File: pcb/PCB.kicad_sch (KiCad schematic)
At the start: 35 parts, among them J1 Conn_01x15, J2 USB_C_Receptacle_USB2.0, J3 Conn_01x15, J4 TC2030, J5 Conn_01x04, SW1 SW_Push, SW2 SW_Push, U1 SN65HVD230, U2 AMS1117-3.3, U3 STM32F103C8T6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

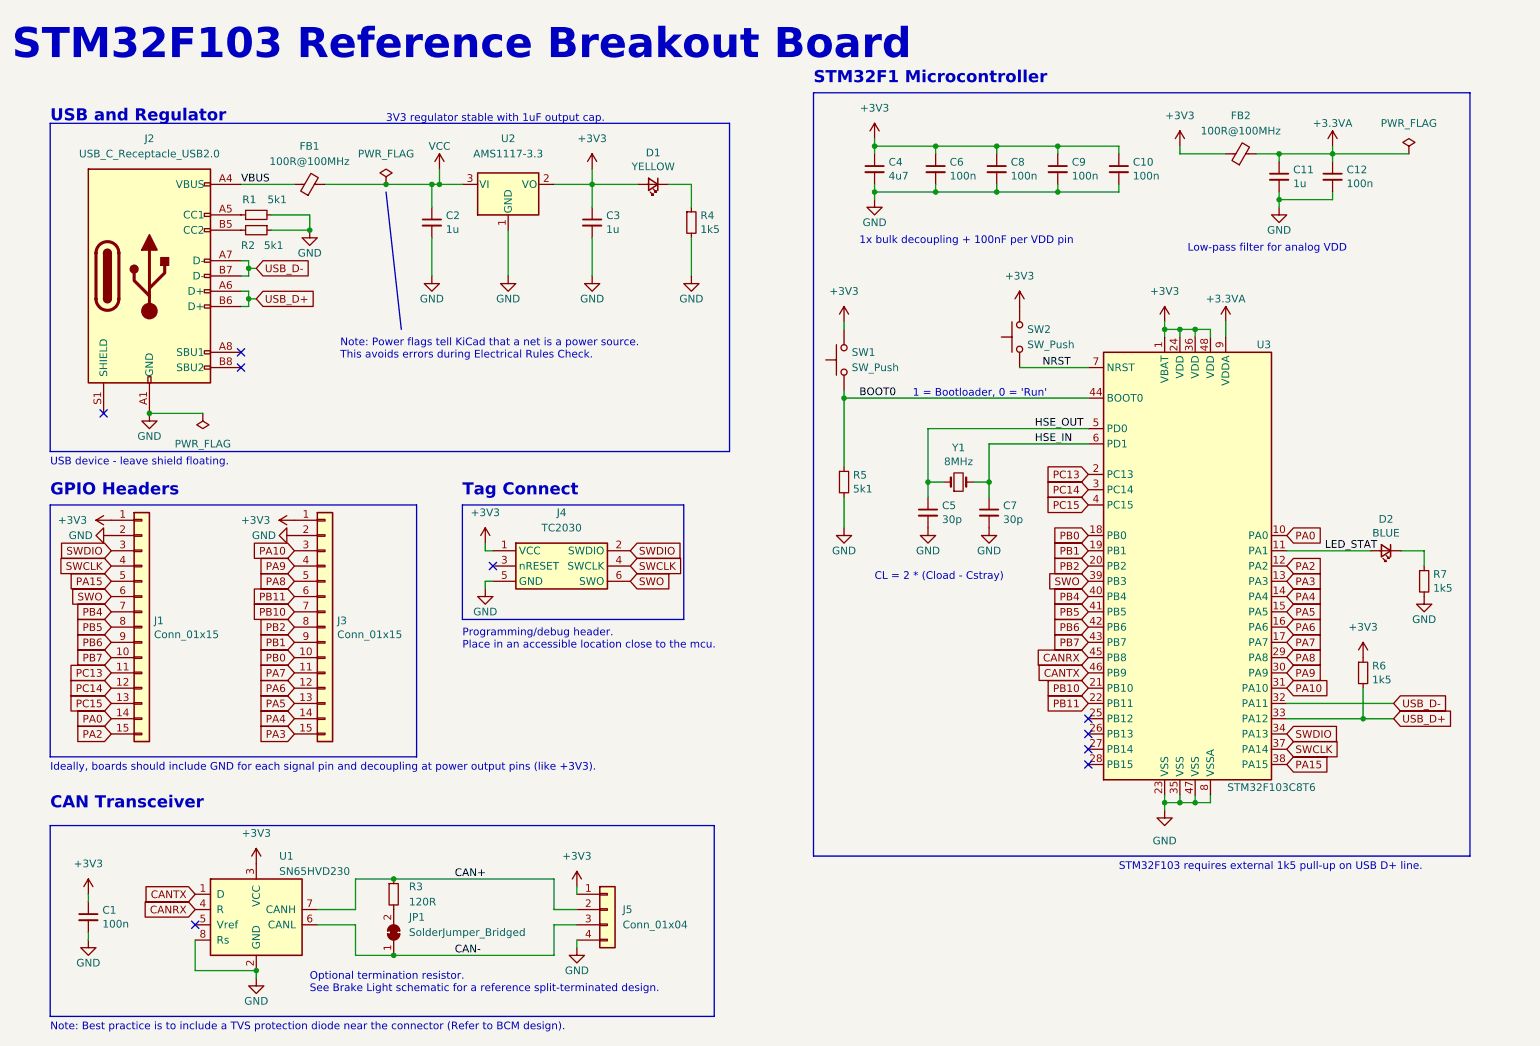
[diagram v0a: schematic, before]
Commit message: Precharge circuit start
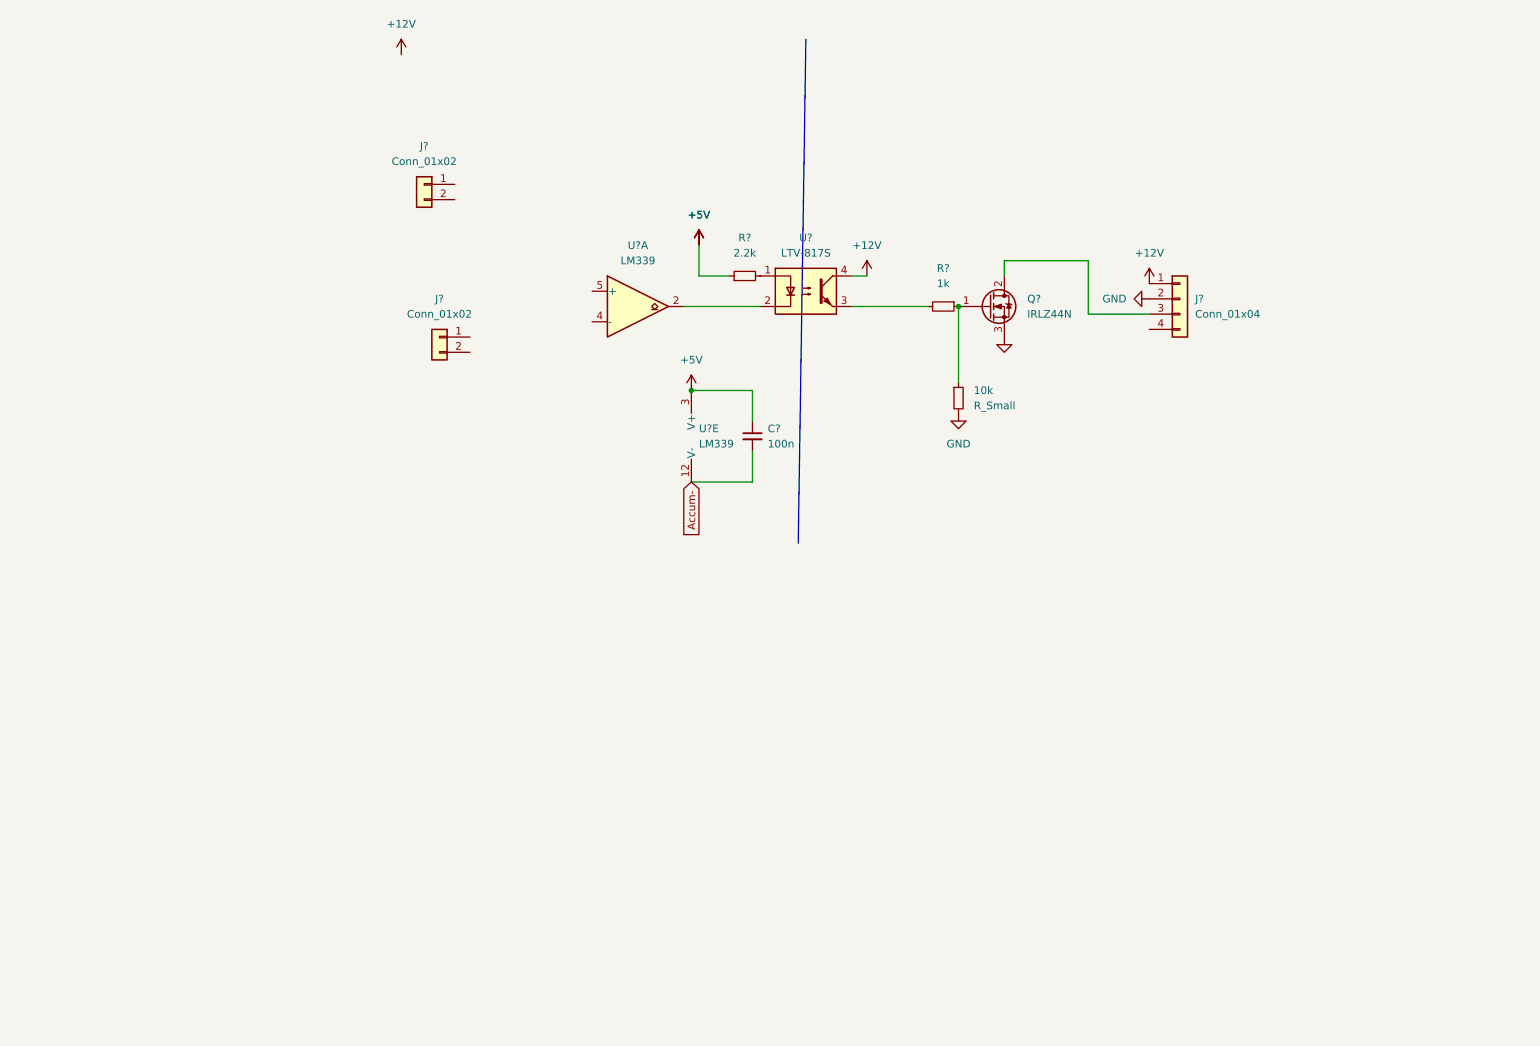
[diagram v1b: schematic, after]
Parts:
- removed C1, C10, C12, C6, C8, C9: 100n, Capacitor_SMD:C_0402_1005Metric, symbol Device:C_Small
- removed C11, C2, C3: 1u, Capacitor_SMD:C_0603_1608Metric, symbol Device:C_Small
- removed C4: 4u7, Capacitor_SMD:C_0603_1608Metric, symbol Device:C_Small
- removed C5, C7: 30p, Capacitor_SMD:C_0402_1005Metric, symbol Device:C_Small
- removed D1: YELLOW, LED_SMD:LED_0603_1608Metric, symbol Device:LED_Small
- removed D2: BLUE, LED_SMD:LED_0603_1608Metric, symbol Device:LED_Small
- removed FB1, FB2: 100R@100MHz, Resistor_SMD:R_0805_2012Metric, symbol Device:FerriteBead_Small
- removed J1, J3: Conn_01x15, Connector_PinHeader_2.54mm:PinHeader_1x15_P2.54mm_Vertical, symbol Connector_Generic:Conn_01x15
- removed J2: USB_C_Receptacle_USB2.0, Connector_USB:USB_C_Receptacle_HRO_TYPE-C-31-M-12, symbol Connector:USB_C_Receptacle_USB2.0
- removed J4: TC2030, Connector:Tag-Connect_TC2030-IDC-NL_2x03_P1.27mm_Vertical, symbol TC2030:TC2030
- removed J5: Conn_01x04, Connector_PinHeader_2.54mm:PinHeader_1x04_P2.54mm_Vertical, symbol Connector_Generic:Conn_01x04
- removed JP1: SolderJumper_Bridged, Jumper:SolderJumper-2_P1.3mm_Bridged_RoundedPad1.0x1.5mm, symbol Jumper:SolderJumper_2_Bridged
- removed R1, R2, R5: 5k1, Resistor_SMD:R_0402_1005Metric, symbol Device:R_Small
- removed R3: 120R, Resistor_SMD:R_0402_1005Metric, symbol Device:R_Small
- removed R4, R6, R7: 1k5, Resistor_SMD:R_0402_1005Metric, symbol Device:R_Small
- removed SW1, SW2: SW_Push, Button_Switch_SMD:SW_Push_1P1T_NO_CK_KSC7xxJ, symbol Switch:SW_Push
- removed U1: SN65HVD230, Package_SO:SOIC-8_3.9x4.9mm_P1.27mm, symbol Interface_CAN_LIN:SN65HVD230
- removed U2: AMS1117-3.3, Package_TO_SOT_SMD:SOT-223-3_TabPin2, symbol Regulator_Linear:AMS1117-3.3
- removed U3: STM32F103C8T6, Package_QFP:LQFP-48_7x7mm_P0.5mm, symbol MCU_ST_STM32F1:STM32F103C8Tx
- removed Y1: 8MHz, Crystal:Crystal_SMD_5032-2Pin_5.0x3.2mm, symbol Device:Crystal_Small
- added 10k: R_Small, symbol Device:R_Small
- added C?: 100n, symbol Device:C_Small
- added J? (x2): Conn_01x02, symbol Connector_Generic:Conn_01x02
- added J?: Conn_01x04, symbol Connector_Generic:Conn_01x04
- added Q?: IRLZ44N, Package_TO_SOT_THT:TO-220-3_Vertical, symbol Transistor_FET:IRLZ44N
- added R?: 1k, symbol Device:R_Small
- added R?: 2.2k, symbol Device:R_Small
- added U? (x2): LM339, symbol Comparator:LM339
- added U?: LTV-817S, Package_DIP:SMDIP-4_W9.53mm, symbol Isolator:LTV-817S
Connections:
- net GND: now also 10k.2, J?.2 (Pin_2), Q?.3 (S)
- new net: 10k.1, Q?.1 (G), R?.1
- new net: J?.3 (Pin_3), Q?.2 (D)
- new net: R?.2, U?.3
- new net: R?.2, U?.1
- new net: U?.2, U?.2
- new net +12V: J?.1 (Pin_1), U?.4
- new net +5V: C?.1, R?.1, U?.3 (V+)
- new net Accum-: C?.2, U?.12 (V-)
- no-connect marks 9 -> 0
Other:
- note removed: "1 = Bootloader, 0 = 'Run'"
- note removed: "1x bulk decoupling + 100nF per VDD pin"
- note removed: "3V3 regulator stable with 1uF output cap."
- note removed: "CAN Transceiver"
- note removed: "CL = 2 * (Cload - Cstray)"
- note removed: "GPIO Headers"
- note removed: "Ideally, boards should include GND for each signal pin and decoupling at power output pins (like +3V3)."
- note removed: "Low-pass filter for analog VDD"
- note removed: "Note: Best practice is to include a TVS protection diode near the connector (Refer to BCM design)."
- note removed: "Note: Power flags tell KiCad that a net is a power source. This avoids errors during Electrical Rules Check."
- note removed: "Optional termination resistor. See Brake Light schematic for a reference split-terminated design."
- note removed: "Programming/debug header. Place in an accessible location close to the mcu."
- note removed: "STM32F1 Microcontroller"
- note removed: "STM32F103 Reference Breakout Board"
- note removed: "STM32F103 requires external 1k5 pull-up on USB D+ line."
- note removed: "Tag Connect"
- note removed: "USB and Regulator"
- note removed: "USB device - leave shield floating."
- title: STM32F103 Reference Breakout Board -> Precharge circuit

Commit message: Precharge PCB update
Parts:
- added D? (x2): D_Zener, symbol Device:D_Zener
- added K?: DBT71205U, DBT71205U, symbol DBT71205U:DBT71205U
- added K?: AZDC6, symbol AZDC6:AZDC6
- added R? (x2): R_Small, symbol Device:R_Small
- added R?: 100k, symbol Device:R_Small
- added R? (x4): 5M, symbol Device:R_Small
- added R?: 110k, symbol Device:R_Small
- added U?: VRB1205YMD-6WR3, symbol VRB1205YMD-6WR3:VRB1205YMD-6WR3
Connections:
- net Accum- is gone; now on net TS-: C?.2, U?.12 (V-)
- net +12V: now also K?.4 (+), K?.5, U?.2 (Vin)
- net +5V: now also U?.3 (+Vo)
- net GND: now also K?.3 (-), K?.6, U?.1 (GND)
- net TS+: now reaches J?.1 (Pin_1)
- net TS+: now also R?.1, R?.1
- net TS-: now reaches J?.2 (Pin_2)
- net TS-: now also D?.2 (A), D?.2 (A), R?.2, R?.2, U?.5 (-Vo)
- net Precharge: now reaches J?.1 (Pin_1)
- net Precharge: now also K?.4, R?.1, R?.1
- net Discharge: now reaches J?.2 (Pin_2)
- net Discharge: now also K?.2 (NC)
- net at U?.4 (-): now also D?.1 (K), R?.1, R?.2
- net at U?.5 (+): now also D?.1 (K), R?.1, R?.2
- new net: K?.1 (COM), R?.2
- new net: K?.1, R?.2
- new net: R?.1, R?.2 (x2)
- new net: K?.2, K?.3
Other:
- moved on the sheet: 10k, C?, J?, Q?, R?, U?, U?A, U?E

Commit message: Updated PCB Design
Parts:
- removed D? (x2): D_Zener, symbol Device:D_Zener
- removed U?: VRB1205YMD-6WR3, symbol VRB1205YMD-6WR3:VRB1205YMD-6WR3
- added D1, D2: SMAJ15CA, Diode_SMD:D_SMA, symbol Device:D_TVS
- added U3: VRB1205YMD-15WR3, VRB1205YMD-6WR3:VRB1205YMD-15WR3, symbol VRB1205YMD-6WR3:VRB1205YMD-15WR3
- C1: renamed from C?; footprint (none) -> Capacitor_SMD:C_0603_1608Metric
- J1, J2: renamed from J?; value Conn_01x02 -> TE 770966-2; footprint (none) -> Connector_TE-Connectivity:TE_MATE-N-LOK_1-770966-x_1x02_P4.14mm_Horizontal
- J3: renamed from J?; value Conn_01x04 -> JST B04B-XASK; footprint (none) -> Connector_JST:JST_XA_B04B-XASK-1_1x04_P2.50mm_Vertical
- K1: renamed from K?; footprint (none) -> AZDC6:AZDC6
- Q1: renamed from Q?; footprint Package_TO_SOT_THT:TO-220-3_Vertical -> Package_TO_SOT_SMD:TO-263-3_TabPin2
- R1, R8: renamed from R?; value R_Small -> hsa255k6j; footprint (none) -> hsa255k6j:hsa255k6j
- R10: renamed from R?; footprint (none) -> Resistor_SMD:R_0603_1608Metric
- R11: renamed from 10k; value R_Small -> 10K; footprint (none) -> Resistor_SMD:R_0603_1608Metric
- R2, R3, R4, R5, R6, R7: renamed from R?; footprint (none) -> Resistor_SMD:R_1206_3216Metric
- R9: renamed from R?; value 2.2k -> 680; footprint (none) -> Resistor_SMD:R_0603_1608Metric
- U1: renamed from U?; footprint (none) -> Package_SO:TSSOP-14_4.4x5mm_P0.65mm
- gave numbers to parts that had none: 2
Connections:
- net +12V: now also U3.1 (Ctrl), U3.3 (Vin)
- net +5V: now also U3.4 (+Vo)
- net GND: now also U3.2 (GND)
- net TS-: now also D1.1 (A1), D2.1 (A1), U3.6 (0V)
- net at R6.2, R7.1, U1.4 (-): now also D2.2 (A2)
- net at R3.2, R4.1, U1.5 (+): now also D1.2 (A2)
- no-connect marks 0 -> 2
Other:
- note added: "5M R Ohmite HVC1206T5004JET"

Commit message: pcb update precharge
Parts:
- removed K2: DBT71205U, DBT71205U, symbol DBT71205U:DBT71205U
- added K2: dbt71205u21, dbt71205u:DBT71205U, symbol dbt71205u2:dbt71205u21
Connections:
- net +12V: now also K2.4 (+)
- net Discharge: now also J2.1 (Pin_1), K2.2 (NC); no longer J2.2 (Pin_2)
- net GND: now also K2.3 (-)
- net Precharge: now also J2.2 (Pin_2); no longer J2.1 (Pin_1)
- net at R8.2: now also K2.1 (COM)
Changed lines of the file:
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@@
+    (stroke (width 0) (type default) (color 0 0 0 0))
+  )
+  (wire (pts (xy 129.54 147.32) (xy 129.54 146.05))
     (stroke (width 0) (type default) (color 0 0 0 0))
   )
@@
     (stroke (width 0) (type default) (color 0 0 0 0))
   )
-  (wire (pts (xy 142.24 133.35) (xy 152.4 133.35))
+  (wire (pts (xy 142.24 133.35) (xy 156.21 133.35))
     (stroke (width 0) (type default) (color 0 0 0 0))
   )
@@
   (global_label "TS+" (shape input) (at 36.83 31.75 0) (fields_autoplaced)
     (effects (font (size 1.27 1.27)) (justify left))
-    (property "Intersheet References" "${INTERSHEET_REFS}" (id 0) (at 42.9926 31.6706 0)
+    (property "Intersheet References" "${INTERSHEET_REFS}" (id 0) (at 42.9926 31.8294 0)
       (effects (font (size 1.27 1.27)) (justify left) hide)
     )
@@
     )
   )
-  (global_label "Precharge" (shape input) (at 38.1 85.09 0) (fields_autoplaced)
+  (global_label "Precharge" (shape input) (at 38.1 87.63 0) (fields_autoplaced)
     (effects (font (size 1.27 1.27)) (justify left))
-    (property "Intersheet References" "${INTERSHEET_REFS}" (id 0) (at 50.0683 85.0106 0)
+    (property "Intersheet References" "${INTERSHEET_REFS}" (id 0) (at 50.0683 87.5506 0)
       (effects (font (size 1.27 1.27)) (justify left) hide)
     )
   )
-  (global_label "Discharge" (shape input) (at 38.1 87.63 0) (fields_autoplaced)
+  (global_label "Discharge" (shape input) (at 38.1 85.09 0) (fields_autoplaced)
     (effects (font (size 1.27 1.27)) (justify left))
-    (property "Intersheet References" "${INTERSHEET_REFS}" (id 0) (at 49.8264 87.5506 0)
+    (property "Intersheet References" "${INTERSHEET_REFS}" (id 0) (at 49.8264 85.0106 0)
       (effects (font (size 1.27 1.27)) (justify left) hide)
     )
@@
   (global_label "TS-" (shape input) (at 36.83 34.29 0) (fields_autoplaced)
     (effects (font (size 1.27 1.27)) (justify left))
-    (property "Intersheet References" "${INTERSHEET_REFS}" (id 0) (at 42.9926 34.2106 0)
+    (property "Intersheet References" "${INTERSHEET_REFS}" (id 0) (at 42.9926 34.3694 0)
       (effects (font (size 1.27 1.27)) (justify left) hide)
     )
@@
     )
   )
-  (global_label "Discharge" (shape input) (at 152.4 133.35 0) (fields_autoplaced)
+  (global_label "Discharge" (shape input) (at 156.21 133.35 0) (fields_autoplaced)
     (effects (font (size 1.27 1.27)) (justify left))
-    (property "Intersheet References" "${INTERSHEET_REFS}" (id 0) (at 164.1264 133.2706 0)
+    (property "Intersheet References" "${INTERSHEET_REFS}" (id 0) (at 167.9364 133.2706 0)
       (effects (font (size 1.27 1.27)) (justify left) hide)
     )
@@
     )
   )
-  (symbol (lib_id "DBT71205U:DBT71205U") (at 116.84 133.35 0) (unit 1)
-    (in_bom yes) (on_board yes) (fields_autoplaced)
-    (property "Reference" "K2" (id 0) (at 143.51 129.0193 0))
-    (property "Value" "DBT71205U" (id 1) (at 143.51 131.5593 0))
-    (property "Footprint" "DBT71205U" (id 2) (at 138.43 125.73 0)
-      (effects (font (size 1.27 1.27)) (justify left) hide)
-    )
-    (property "Datasheet" "https://www.mouser.de/datasheet/2/657/cynergy3_db_ul_v3-1892211.pdf" (id 3) (at 138.43 128.27 0)
-      (effects (font (size 1.27 1.27)) (justify left) hide)
-    )
-    (property "Description" "RELAY REED SPST-NC 5KV12V" (id 4) (at 138.43 130.81 0)
-      (effects (font (size 1.27 1.27)) (justify left) hide)
-    )
-    (property "Height" "18.5" (id 5) (at 138.43 133.35 0)
-      (effects (font (size 1.27 1.27)) (justify left) hide)
-    )
-    (property "Mouser Part Number" "285-DBT71205U" (id 6) (at 138.43 135.89 0)
-      (effects (font (size 1.27 1.27)) (justify left) hide)
-    )
-    (property "Mouser Price/Stock" "https://www.mouser.co.uk/ProductDetail/Cynergy3/DBT71205U?qs=OlC7AqGiEDmpzAJpsZ9Ytg%3D%3D" (id 7) (at 138.43 138.43 0)
-      (effects (font (size 1.27 1.27)) (justify left) hide)
-    )
-    (property "Manufacturer_Name" "Cynergy3" (id 8) (at 138.43 140.97 0)
-      (effects (font (size 1.27 1.27)) (justify left) hide)
-    )
-    (property "Manufacturer_Part_Number" "DBT71205U" (id 9) (at 138.43 143.51 0)
-      (effects (font (size 1.27 1.27)) (justify left) hide)
-    )
-    (pin "1")
-    (pin "2")
-    (pin "3")
-    (pin "4")
-  )
   (symbol (lib_id "power:+12V") (at 168.91 82.55 0) (unit 1)
     (in_bom yes) (on_board yes) (fields_autoplaced)
@@
     (pin "2")
   )
-  (symbol (lib_id "power:GND") (at 129.54 146.05 0) (unit 1)
-    (in_bom yes) (on_board yes) (fields_autoplaced)
-    (property "Reference" "#PWR04" (id 0) (at 129.54 152.4 0)
-      (effects (font (size 1.27 1.27)) hide)
-    )
-    (property "Value" "GND" (id 1) (at 129.54 151.13 0))
-    (property "Footprint" "" (id 2) (at 129.54 146.05 0)
-      (effects (font (size 1.27 1.27)) hide)
-    )
-    (property "Datasheet" "" (id 3) (at 129.54 146.05 0)
+  (symbol (lib_id "power:GND") (at 129.54 147.32 0) (unit 1)
+    (in_bom yes) (on_board yes) (fields_autoplaced)
+    (property "Reference" "#PWR04" (id 0) (at 129.54 153.67 0)
+      (effects (font (size 1.27 1.27)) hide)
+    )
+    (property "Value" "GND" (id 1) (at 129.54 152.4 0))
+    (property "Footprint" "" (id 2) (at 129.54 147.32 0)
+      (effects (font (size 1.27 1.27)) hide)
+    )
+    (property "Datasheet" "" (id 3) (at 129.54 147.32 0)
       (effects (font (size 1.27 1.27)) hide)
     )
@@
     (pin "1")
     (pin "2")
+  )
+  (symbol (lib_id "dbt71205u2:dbt71205u21") (at 113.03 128.27 0) (unit 1)
+    (in_bom yes) (on_board yes) (fields_autoplaced)
+    (property "Reference" "K2" (id 0) (at 144.78 129.0193 0))
+    (property "Value" "dbt71205u21" (id 1) (at 144.78 131.5593 0))
+    (property "Footprint" "dbt71205u:DBT71205U" (id 2) (at 113.03 128.27 0)
+      (effects (font (size 1.27 1.27)) hide)
+    )
+    (property "Datasheet" "" (id 3) (at 113.03 128.27 0)
+      (effects (font (size 1.27 1.27)) hide)
+    )
+    (pin "1")
+    (pin "2")
+    (pin "3")
+    (pin "4")
   )
   (symbol (lib_id "power:GND") (at 189.23 76.2 0) (unit 1)
@@
       (reference "K1") (unit 1) (value "AZDC6") (footprint "AZDC6:AZDC6")
     )
-    (path "/07d5fb5b-8774-4277-b8b4-525d92b5a5b0"
-      (reference "K2") (unit 1) (value "DBT71205U") (footprint "DBT71205U")
+    (path "/b3f0aa41-acc2-4d94-97fe-f1817c949dfa"
+      (reference "K2") (unit 1) (value "dbt71205u21") (footprint "dbt71205u:DBT71205U")
     )
     (path "/e787d86b-2b5e-40e9-9bbd-afb4cb4e8fef"

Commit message: bbs home
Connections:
- net AIR: now reaches J3.3 (Pin_3), Q1.2 (D)
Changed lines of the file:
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@@
     (effects (font (size 1.27 1.27)) (justify right bottom))
+  )
+  (label "AIR" (at 205.74 72.39 0)
+    (effects (font (size 1.27 1.27)) (justify left bottom))
   )
   (global_label "TS+" (shape input) (at 46.99 144.78 180) (fields_autoplaced)
